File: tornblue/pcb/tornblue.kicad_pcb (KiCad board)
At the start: 2 copper layers, 140.7 x 102.9 mm, 78 parts, among them J1 BATT, J2 SWD, J3 BREAKOUT, J4 USB C - USB2.0, Q1 AO3401A, Q2 AO3401A, SW1 SW_Push, SW10 SW_Push, SW11 SW_Push, SW12 SW_Push, SW13 SW_Push, SW14 SW_Push, SW15 SW_Push, SW16 SW_Push, SW17 SW_Push, SW18 SW_Push, SW19 EC11, SW2 SW_Push, SW20 SW_Push, SW21 SW_Push, SW22 EC11, SW23 RESET, SW3 SW_Push, SW4 SW_Push, SW5 SW_Push, SW6 SW_Push, SW7 SW_Push, SW8 SW_Push, SW9 SW_Push, U1 XC6220, U2 TP4056, U3 nRF52840_holyiot_18010, U4 SRV05-4

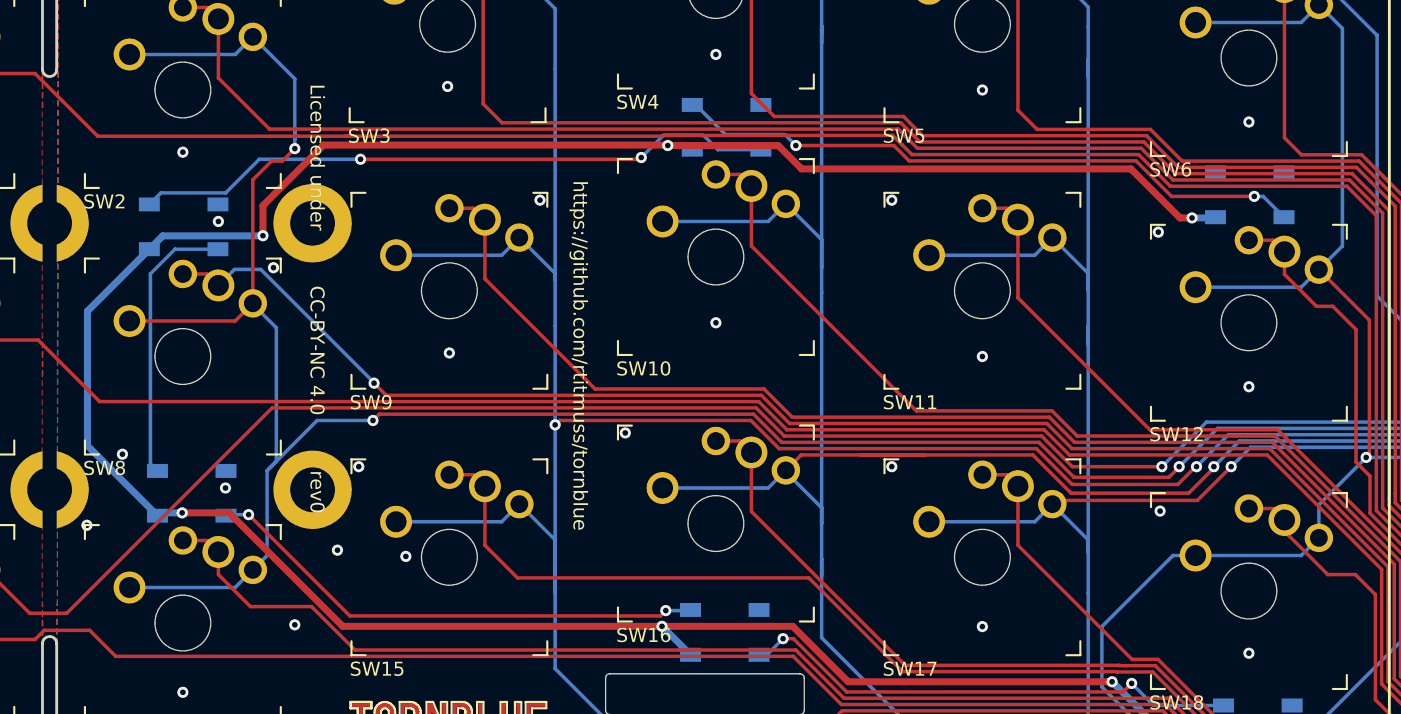
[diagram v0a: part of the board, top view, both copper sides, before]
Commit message: Move underglow leds up 1mm
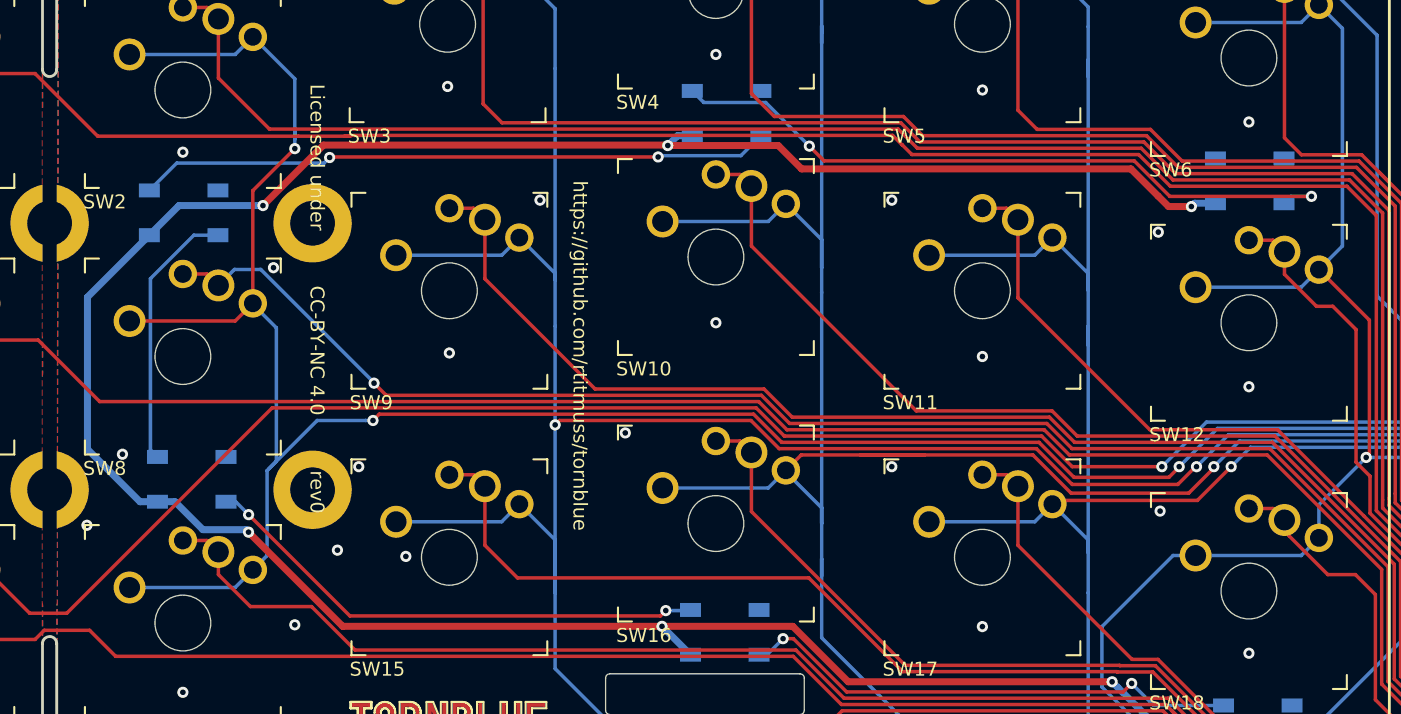
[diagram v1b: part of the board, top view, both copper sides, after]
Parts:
- moved D14 1.00 mm to (110.7, 92.5)
- moved D15 1.00 mm to (186.4, 71.1)
- moved D16 1.00 mm to (149.0, 66.3)
- moved D17 1.00 mm to (110.2, 73.4)
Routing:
- net Net-(D15-Pad4): track 45.7 -> 49.5 mm
- net Net-(D16-Pad4): track 46.2 -> 45.3 mm
- net EXT_VCC: track 218.8 -> 218.0 mm
- net Net-(D14-Pad2): track 19.9 -> 19.1 mm
- net GND: vias 45 -> 43

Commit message: Add battery pins + silk screen fixes
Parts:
- removed the R10 at (212.4, 55.0)
- added J5: BATT_PIN, Connector_PinHeader_2.54mm:PinHeader_1x02_P2.54mm_Vertical, F.Cu at (210.7, 55.0)
- added R9: 5.1k, Resistor_SMD:R_0805_2012Metric, F.Cu at (211.9, 57.9)
- moved R10 1.76 mm to (211.9, 59.9)
- turned R3 to 180 degrees
- renumbered R9 to R10
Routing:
- net VBAT: track 47.3 -> 54.0 mm, vias 1 -> 2
- net ROW2: track 29.8 -> 32.3 mm
- net Net-(R5-Pad2): track 7.57 -> 5.80 mm, vias 2 -> 0
- net Net-(C3-Pad1): track 29.5 -> 30.4 mm
- net Net-(D25-Pad1): track 3.99 -> 3.16 mm
- net +3V3: track 57.2 -> 58.0 mm
- net Net-(J4-PadB5): track 12.0 -> 11.3 mm
- net +5V: track 81.6 -> 81.5 mm, vias 4 -> 2
- net GND: vias 43 -> 44

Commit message: Add power switch
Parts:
- added SW24: SW_SPST, Button_Switch_SMD:SW_SPDT_PCM12, F.Cu at (190.4, 52.9)
- SW23: value RESET -> RST
- moved SW23 5.32 mm to (181.0, 52.1)
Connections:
- C4 pad 1: +3V3 -> Net-(C4-Pad1)
- U1 pad 5: +3V3 -> Net-(C4-Pad1)
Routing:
- net Net-(C4-Pad1): track 0.00 -> 29.3 mm, vias 0 -> 2
- net +3V3: track 58.0 -> 77.8 mm, vias 2 -> 4
- net Net-(SW23-Pad1): track 53.0 -> 58.0 mm
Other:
- board text added: "OFF"
- board text added: "ON"
